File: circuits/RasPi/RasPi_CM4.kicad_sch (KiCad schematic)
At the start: 0 parts

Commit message: PDFプロット
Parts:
- added C37, C39, C40, C41, C42, C43, C44: 0.1uF, Capacitor_SMD:C_0402_1005Metric, symbol Device:C
- added J10: Conn_01x03_MountingPin, Connector_Molex:Molex_PicoBlade_53261-0371_1x03-1MP_P1.25mm_Horizontal, symbol Connector_Generic_MountingPin:Conn_01x03_MountingPin
- added J9: Conn_01x04_MountingPin, Connector_Molex:Molex_PicoBlade_53261-0471_1x04-1MP_P1.25mm_Horizontal, symbol Connector_Generic_MountingPin:Conn_01x04_MountingPin
- added R92: 10k, Resistor_SMD:R_0402_1005Metric, symbol Device:R
- added SW5: SW_SPDT, MyLibrary:SW_Slide_3P_SPDT, symbol Switch:SW_SPDT
- added SW7: SW_SPST, Button_Switch_SMD:SW_SPST_Omron_B3FS-100xP, symbol Switch:SW_SPST
- added U6: SBC_RPi-CM4, MyLibrary:SBC_RPi-CM4, symbol MyLibrary:SBC_RPi-CM4
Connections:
- new net +3.3V: R92.1
- new net +5V: C37.1, C39.1, C40.1, C41.1, C42.1, C44.1, J10.2 (Pin_2), J9.2 (Pin_2), U6.77 (+5V(INPUT)), U6.79 (+5V(INPUT)__1), U6.81 (+5V(INPUT)__2), U6.83 (+5V(INPUT)__3), U6.85 (+5V(INPUT)__4), U6.87 (+5V(INPUT)__5)
- new net CM4_1.8V(OUTPUT)__1: U6.88 (CM4_1.8V(OUTPUT)), U6.90 (CM4_1.8V(OUTPUT)__1)
- new net CM4_3.3V(OUTPUT)__1: U6.78 (GPIO_VREF), U6.84 (CM4_3.3V(OUTPUT)), U6.86 (CM4_3.3V(OUTPUT)__1)
- new net DSI1_CK_N: U6.189 (DSI1_C_P)
- new net DSI1_CK_P: U6.187 (DSI1_C_N)
- new net DSI1_D0_N: U6.175 (DSI1_D0_N)
- new net DSI1_D0_P: U6.177 (DSI1_D0_P)
- new net DSI1_D1_N: U6.181 (DSI1_D1_N)
- new net DSI1_D1_P: U6.183 (DSI1_D1_P)
- new net DSI1_D2_N: U6.193 (DSI1_D2_N)
- new net DSI1_D2_P: U6.195 (DSI1_D2_P)
- new net DSI1_D3_N: U6.194 (DSI1_D3_N)
- new net DSI1_D3_P: U6.196 (DSI1_D3_P)
- new net GLOBAL_EN: SW5.1 (A), U6.99 (GLOBAL_EN)
- new net GNDD: C37.2, C39.2, C40.2, C41.2, C42.2, C43.2, C44.2, J10.1 (Pin_1), J10.MP (MountPin), J9.1 (Pin_1), J9.MP (MountPin), SW5.2 (B), SW7.2 (B), U6.1 (GND), U6.107 (GND__21), U6.108 (GND__22), U6.113 (GND__23), U6.114 (GND__24), U6.119 (GND__25), U6.120 (GND__26), U6.125 (GND__27), U6.126 (GND__28), U6.13 (GND__4), U6.131 (GND__29), U6.132 (GND__30), U6.137 (GND__31), U6.138 (GND__32), U6.14 (GND__5), U6.144 (GND__33), U6.150 (GND__34), U6.155 (GND__35), U6.156 (GND__36), U6.161 (GND__37), U6.162 (GND__38), U6.167 (GND__39), U6.168 (GND__40), U6.173 (GND__41), U6.174 (GND__42), U6.179 (GND__43), U6.180 (GND__44), U6.185 (GND__45), U6.186 (GND__46), U6.191 (GND__47), U6.192 (GND__48), U6.197 (GND__49), U6.198 (GND__50), U6.2 (GND__1), U6.22 (GND__6), U6.23 (GND__7), U6.32 (GND__8), U6.33 (GND__9), U6.42 (GND__10), U6.43 (GND__11), U6.52 (GND__12), U6.53 (GND__13), U6.59 (GND__14), U6.60 (GND__15), U6.65 (GND__16), U6.66 (GND__17), U6.7 (GND__2), U6.71 (GND__18), U6.74 (GND__19), U6.8 (GND__3), U6.98 (GND__20)
- new net LED_nACT: U6.21 (PI_~{LED}_ACTIVITY)
- new net LED_nPWR: U6.95 (PI_LED_~{PWR})
- new net LiDAR_PWM: J10.3 (Pin_3)
- new net PCM_CLK: U6.49 (GPIO18)
- new net PCM_DIN: U6.27 (GPIO20)
- new net PCM_DOUT: U6.25 (GPIO21)
- new net PCM_FS: U6.26 (GPIO19)
- new net RasPiRXx_LiDARTX: J9.4 (Pin_4)
- new net RasPiTXx_LiDARRX: J9.3 (Pin_3)
- new net SD_CLK: U6.57 (SD_CLK)
- new net SD_CMD: U6.62 (SD_CMD)
- new net SD_DAT0: U6.63 (SD_DAT0)
- new net SD_DAT1: U6.67 (SD_DAT1)
- new net SD_DAT2: U6.69 (SD_DAT2)
- new net SD_DAT3: U6.61 (SD_DAT3)
- new net SD_PWR_ON: U6.75 (SD_PWR_ON)
- new net SHDN/BOOT: C43.1, SW7.1 (A), U6.56 (GPIO3)
- new net V_SHDN: R92.2
- no-connect marks 0 -> 61
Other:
- added sheet Ethernet (Ethernet.kicad_sch)
- added sheet FAN (FAN.kicad_sch)
- added sheet SD_Card (SD_Card.kicad_sch)
- added sheet UI_RasPi (UI_RasPi.kicad_sch)
- note added: "Conn to LiDAR"
- note added: "GLOBAL ENABLE Switch"
- note added: "GLOBAL_EN SHDN/BOOT(GPIO3) V_SHDN(電圧監視SHDN)"
- note added: "ShutDown/BOOT Switch"
- note added: "パスコン"

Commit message: panelフットプリント配置
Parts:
- removed J10: Conn_01x03_MountingPin, Connector_Molex:Molex_PicoBlade_53261-0371_1x03-1MP_P1.25mm_Horizontal, symbol Connector_Generic_MountingPin:Conn_01x03_MountingPin
- removed J9: Conn_01x04_MountingPin, Connector_Molex:Molex_PicoBlade_53261-0471_1x04-1MP_P1.25mm_Horizontal, symbol Connector_Generic_MountingPin:Conn_01x04_MountingPin
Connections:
- net RasPiRX0_SerialTX: now reaches U6.51 (GPIO15)
- net RasPiTX0_SerialRX: now reaches U6.55 (GPIO14)
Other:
- added sheet LiDAR (LiDAR.kicad_sch)
- added sheet Serial_Converter (Serial_Converter.kicad_sch)
- note removed: "Conn to LiDAR"

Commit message: シンボル・フットプリントMyLib->TomoshibiLib置き換え
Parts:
- SW5: footprint MyLibrary:SW_Slide_3P_SPDT -> TomoshibiLibrary:SW_Slide_3P_SPDT
- U6: footprint MyLibrary:SBC_RPi-CM4 -> TomoshibiLibrary:SBC_RPi-CM4; symbol MyLibrary:SBC_RPi-CM4 -> TomoshibiLibrary:SBC_RPi-CM4
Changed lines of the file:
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@@
     )
   )
-  (symbol (lib_name "SBC_RPi-CM4_1") (lib_id "MyLibrary:SBC_RPi-CM4") (at 111.76 104.14 0) (unit 1)
+  (symbol (lib_id "TomoshibiLibrary:SBC_RPi-CM4") (at 111.76 104.14 0) (unit 1)
     (in_bom yes) (on_board yes) (dnp no)
     (property "Reference" "U6" (at 88.9 40.64 0)
@@
       (effects (font (size 1.27 1.27)))
     )
-    (property "Footprint" "MyLibrary:SBC_RPi-CM4" (at 111.76 104.14 0)
-      (effects (font (size 1.27 1.27)) (justify bottom) hide)
-    )
-    (property "Datasheet" "" (at 111.76 104.14 0)
-      (effects (font (size 1.27 1.27)) hide)
-    )
-    (property "PARTREV" "2021-10-12" (at 111.76 104.14 0)
-      (effects (font (size 1.27 1.27)) (justify bottom) hide)
-    )
-    (property "MANUFACTURER" "Raspberry Pi" (at 111.76 104.14 0)
-      (effects (font (size 1.27 1.27)) (justify bottom) hide)
-    )
-    (property "MAXIMUM_PACKAGE_HEIGHT" "5.188 mm" (at 111.76 104.14 0)
-      (effects (font (size 1.27 1.27)) (justify bottom) hide)
-    )
-    (property "STANDARD" "Manufacturer Recommendations" (at 111.76 104.14 0)
+    (property "Footprint" "TomoshibiLibrary:SBC_RPi-CM4" (at 104.14 17.78 0)
+      (effects (font (size 1.27 1.27)) (justify bottom) hide)
+    )
+    (property "Datasheet" "" (at 104.14 17.78 0)
+      (effects (font (size 1.27 1.27)) hide)
+    )
+    (property "PARTREV" "2021-10-12" (at 104.14 17.78 0)
+      (effects (font (size 1.27 1.27)) (justify bottom) hide)
+    )
+    (property "MANUFACTURER" "Raspberry Pi" (at 104.14 17.78 0)
+      (effects (font (size 1.27 1.27)) (justify bottom) hide)
+    )
+    (property "MAXIMUM_PACKAGE_HEIGHT" "5.188 mm" (at 104.14 17.78 0)
+      (effects (font (size 1.27 1.27)) (justify bottom) hide)
+    )
+    (property "STANDARD" "Manufacturer Recommendations" (at 104.14 17.78 0)
       (effects (font (size 1.27 1.27)) (justify bottom) hide)
     )
@@
       (effects (font (size 1.27 1.27)) (justify left))
     )
-    (property "Footprint" "MyLibrary:SW_Slide_3P_SPDT" (at 38.1 35.56 0)
-      (effects (font (size 1.27 1.27)) hide)
-    )
+    (property "Footprint" "TomoshibiLibrary:SW_Slide_3P_SPDT" (at 38.1 35.56 0)
+      (effects (font (size 1.27 1.27)) hide)
+    )

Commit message: 更新
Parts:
- removed U6: SBC_RPi-CM4, TomoshibiLibrary:SBC_RPi-CM4, symbol TomoshibiLibrary:SBC_RPi-CM4
- added U1: SBC_RPi-CM4, TomoshibiLibrary:SBC_RPi-CM4, symbol TomoshibiLibrary:SBC_RPi-CM4
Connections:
- net +5V: now also U1.77 (+5V(INPUT)), U1.79 (+5V(INPUT)__1), U1.81 (+5V(INPUT)__2), U1.83 (+5V(INPUT)__3), U1.85 (+5V(INPUT)__4), U1.87 (+5V(INPUT)__5)
- net CM4_1.8V(OUTPUT)__1: now also U1.88 (CM4_1.8V(OUTPUT)), U1.90 (CM4_1.8V(OUTPUT)__1)
- net CM4_3.3V(OUTPUT)__1: now also U1.78 (GPIO_VREF), U1.84 (CM4_3.3V(OUTPUT)), U1.86 (CM4_3.3V(OUTPUT)__1)
- net DSI1_CK_N: now also U1.187 (DSI1_C_N)
- net DSI1_CK_P: now also U1.189 (DSI1_C_P)
- net DSI1_D0_N: now also U1.175 (DSI1_D0_N)
- net DSI1_D0_P: now also U1.177 (DSI1_D0_P)
- net DSI1_D1_N: now also U1.181 (DSI1_D1_N)
- net DSI1_D1_P: now also U1.183 (DSI1_D1_P)
- net DSI1_D2_N: now also U1.193 (DSI1_D2_N)
- net DSI1_D2_P: now also U1.195 (DSI1_D2_P)
- net DSI1_D3_N: now also U1.194 (DSI1_D3_N)
- net DSI1_D3_P: now also U1.196 (DSI1_D3_P)
- net ETH_LEDG: now also U1.17 (ETHERNET_~{LED2})
- net ETH_LEDY: now also U1.15 (ETHERNET_~{LED3})
- net GLOBAL_EN: now also SW5.3 (C), U1.99 (GLOBAL_EN); no longer SW5.1 (A)
- net GNDD: now also U1.1 (GND), U1.107 (GND__21), U1.108 (GND__22), U1.113 (GND__23), U1.114 (GND__24), U1.119 (GND__25), U1.120 (GND__26), U1.125 (GND__27), U1.126 (GND__28), U1.13 (GND__4), U1.131 (GND__29), U1.132 (GND__30), U1.137 (GND__31), U1.138 (GND__32), U1.14 (GND__5), U1.144 (GND__33), U1.150 (GND__34), U1.155 (GND__35), U1.156 (GND__36), U1.161 (GND__37), U1.162 (GND__38), U1.167 (GND__39), U1.168 (GND__40), U1.173 (GND__41), U1.174 (GND__42), U1.179 (GND__43), U1.180 (GND__44), U1.185 (GND__45), U1.186 (GND__46), U1.191 (GND__47), U1.192 (GND__48), U1.197 (GND__49), U1.198 (GND__50), U1.2 (GND__1), U1.22 (GND__6), U1.23 (GND__7), U1.32 (GND__8), U1.33 (GND__9), U1.42 (GND__10), U1.43 (GND__11), U1.52 (GND__12), U1.53 (GND__13), U1.59 (GND__14), U1.60 (GND__15), U1.65 (GND__16), U1.66 (GND__17), U1.7 (GND__2), U1.71 (GND__18), U1.74 (GND__19), U1.8 (GND__3), U1.98 (GND__20)
- net LED_nACT: now also U1.21 (PI_~{LED}_ACTIVITY)
- net LED_nPWR: now also U1.95 (PI_LED_~{PWR})
- net PCM_CLK: now also U1.49 (GPIO18)
- net PCM_DIN: now also U1.27 (GPIO20)
- net PCM_DOUT: now also U1.25 (GPIO21)
- net PCM_FS: now also U1.26 (GPIO19)
- net RasPiRX0_SerialTX: now also U1.51 (GPIO15)
- net RasPiTX0_SerialRX: now also U1.55 (GPIO14)
- net SD_CLK: now also U1.57 (SD_CLK)
- net SD_CMD: now also U1.62 (SD_CMD)
- net SD_DAT0: now also U1.63 (SD_DAT0)
- net SD_DAT1: now also U1.67 (SD_DAT1)
- net SD_DAT2: now also U1.69 (SD_DAT2)
- net SD_DAT3: now also U1.61 (SD_DAT3)
- net SD_PWR_ON: now also U1.75 (SD_PWR_ON)
- net SHDN/BOOT: now also U1.56 (GPIO3)
- net TRD0_N: now also U1.10 (ETHERNET_PAIR0_N)
- net TRD0_P: now also U1.12 (ETHERNET_PAIR0_P)
- net TRD1_N: now also U1.6 (ETHERNET_PAIR1_N)
- net TRD1_P: now also U1.4 (ETHERNET_PAIR1_P)
- no-connect marks 61 -> 65

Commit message: raspi基板回路図
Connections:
- net +3.3V is gone; now on net CM4_3.3V(OUTPUT)__1: R92.1
- net LiDAR_PWM: now also U1.80 (SCL0)
- net RasPiRX5_LiDARTX: now reaches U1.28 (GPIO13)
- net MOSI4: now reaches U1.30 (GPIO6)
- net RasPiTX5_LiDARRX: now reaches U1.31 (GPIO12)
- net MISO4: now reaches U1.34 (GPIO5)
- net SCLK4: now reaches U1.37 (GPIO7)
- net SCLK0: now reaches U1.38 (GPIO11)
- net CS0_MCU: now reaches U1.39 (GPIO8)
- net MISO0: now reaches U1.40 (GPIO9)
- net MOSI0: now reaches U1.44 (GPIO10)
- net CS4_FPGA: now reaches U1.54 (GPIO4)
- no-connect marks 65 -> 88
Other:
- sheet UI_RasPi ports: added LED_B0, LED_B1; removed none
- moved on the sheet: R92

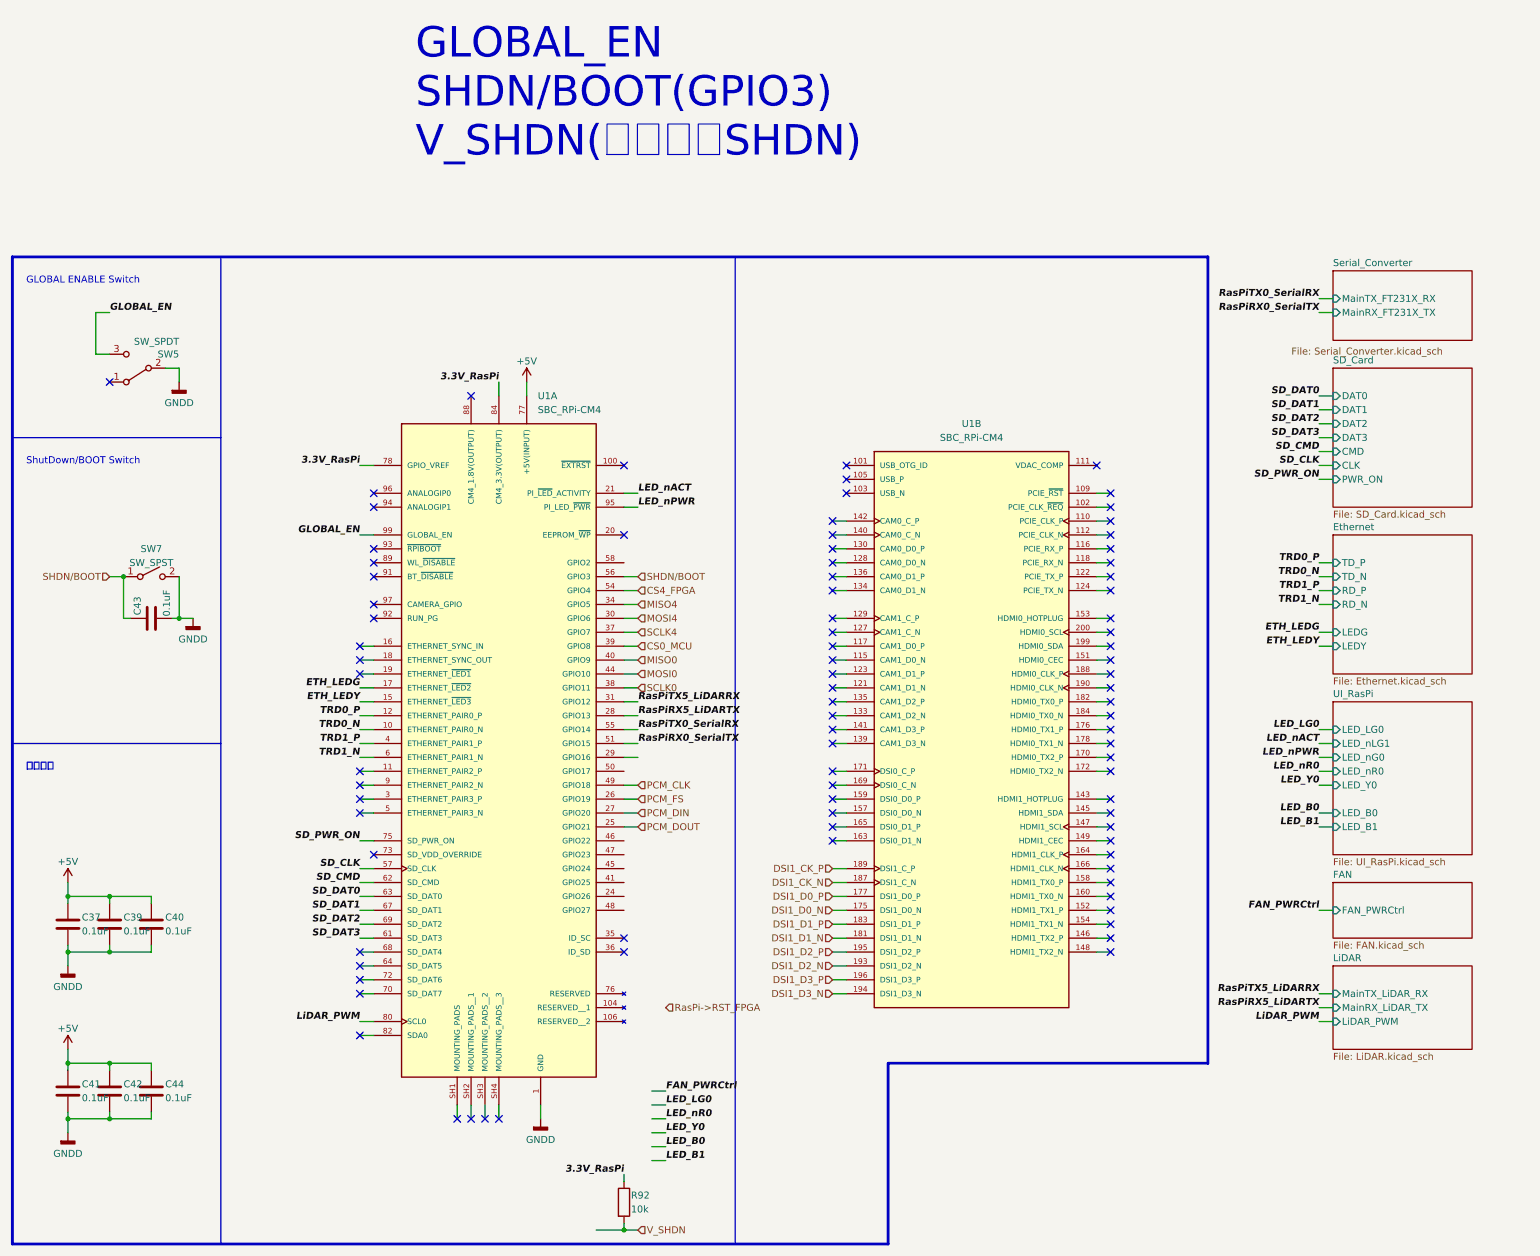
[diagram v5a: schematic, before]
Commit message: 発注第2弾
RasPi発注
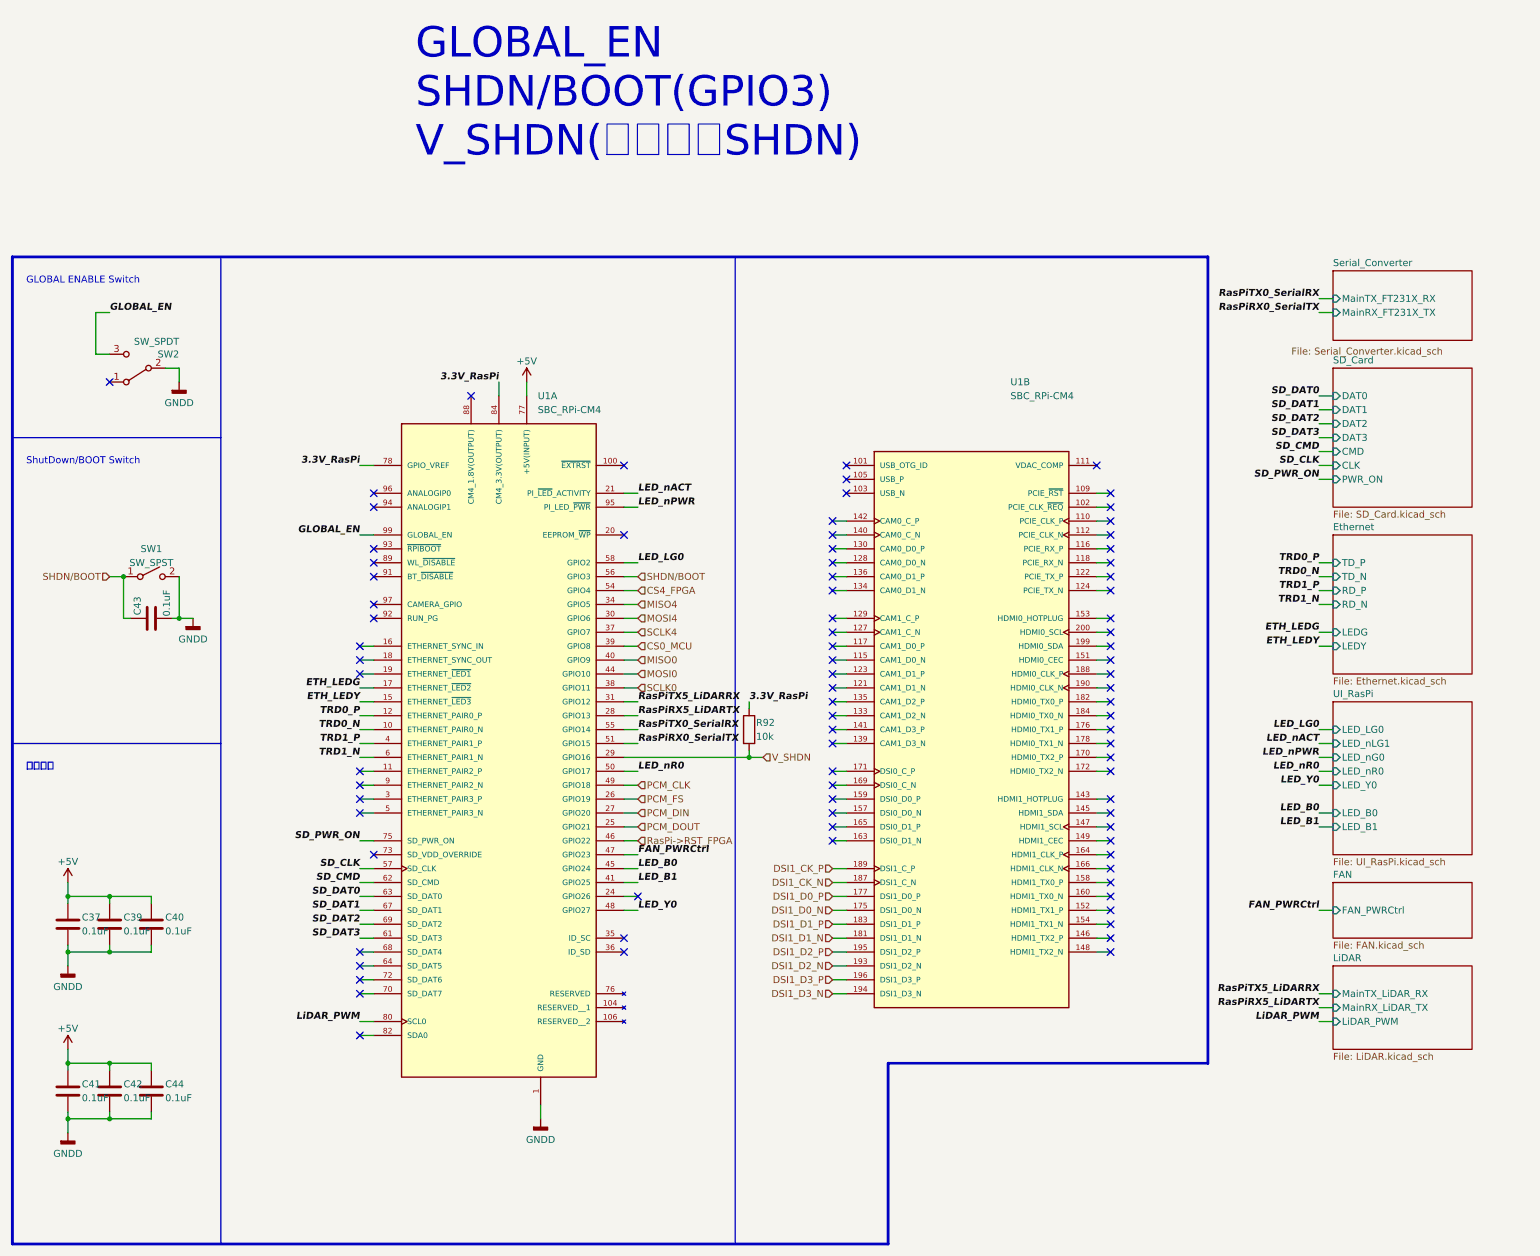
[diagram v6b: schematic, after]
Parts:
- U1: footprint TomoshibiLibrary:SBC_RPi-CM4 -> TomoshibiLibrary:SBC_RPi-CM4_NoMountingHoles
- renumbered SW7 to SW1, SW5 to SW2
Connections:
- net FAN_PWRCtrl: now also U1.47 (GPIO23)
- net LED_B0: now also U1.45 (GPIO24)
- net LED_B1: now also U1.41 (GPIO25)
- net LED_LG0: now also U1.58 (GPIO2)
- net LED_Y0: now also U1.48 (GPIO27)
- net LED_nR0: now also U1.50 (GPIO17)
- net RasPi->RST_FPGA: now also U1.46 (GPIO22)
- net V_SHDN: now also U1.29 (GPIO16)
- no-connect marks 88 -> 85
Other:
- moved on the sheet: R92
